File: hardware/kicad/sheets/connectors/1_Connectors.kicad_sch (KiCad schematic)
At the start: 27 parts, among them CN12 5017, CN13 B4B-PH-K-S(LF)(SN), Q68 CSD17577Q5A, U155 MT9700-N, U156 150uF, U181 LM5050MKX-1/NOPB, U81 DS1021-2x13SF11-B

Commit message: reorganized
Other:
- sheet Connectors 12V JST renamed 12V JST Outputs
- sheet Connectors 5V JST renamed 5V JST Outputs
- sheet Connectors ESC renamed ESC Connectors
- sheet Connectors Wire To Board renamed Board IO Connectors
- title: Connectors -> External Connectors
- moved on the sheet: ESC-6V1, H3, H4

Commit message: before final cleanup
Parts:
- renumbered C235 to C83, C267 to C84, C234 to C85, C274 to C86, C275 to C87, C236 to C88, CN12 to CN6, CN13 to CN7, D76 to D25, ESC-6V2 to ESC-6V1, ESC-6V1 to ESC-6V2, H3 to H5, H4 to H6, Q68 to Q14, R445 to R133, R426 to R134, R427 to R135, R514 to R136, R515 to R137, R513 to R138, U157 to U47, U155 to U48, U181 to U49, U156 to U50, U81 to U51

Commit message: pre kicad footprints
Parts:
- C84: footprint 5v rail sm-easyedapro:CAP-TH_BD13.0-P5.00-D0.6-FD -> Capacitor_THT:CP_Radial_D13.0mm_P5.00mm
- ESC-6V1: footprint 5v rail sm-easyedapro:HDR-TH_2P-P2.54-V-M -> Connector_PinHeader_2.54mm:PinHeader_2x01_P2.54mm_Vertical
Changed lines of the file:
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@@
 	(wire
 		(pts
-			(xy 101.6 64.77) (xy 142.24 64.77)
+			(xy 101.6 66.04) (xy 102.87 66.04)
 		)
 		(stroke
@@
 	(wire
 		(pts
+			(xy 100.33 97.79) (xy 142.24 97.79)
+		)
+		(stroke
+			(width 0)
+			(type default)
+		)
+	)
+	(wire
+		(pts
+			(xy 102.87 66.04) (xy 102.87 64.77)
+		)
+		(stroke
+			(width 0)
+			(type default)
+		)
+	)
+	(wire
+		(pts
 			(xy 165.1 247.65) (xy 165.1 255.27)
 		)
@@
 	(wire
 		(pts
-			(xy 101.6 97.79) (xy 142.24 97.79)
+			(xy 96.52 99.06) (xy 100.33 99.06)
 		)
 		(stroke
@@
 	(wire
 		(pts
+			(xy 100.33 99.06) (xy 100.33 97.79)
+		)
+		(stroke
+			(width 0)
+			(type default)
+		)
+	)
+	(wire
+		(pts
 			(xy 138.43 77.47) (xy 138.43 74.93)
 		)
@@
 	(wire
 		(pts
+			(xy 102.87 59.69) (xy 142.24 59.69)
+		)
+		(stroke
+			(width 0)
+			(type default)
+		)
+	)
+	(wire
+		(pts
 			(xy 105.41 200.66) (xy 100.33 200.66)
 		)
@@
 	(wire
 		(pts
-			(xy 101.6 92.71) (xy 142.24 92.71)
+			(xy 97.79 91.44) (xy 100.33 91.44)
 		)
 		(stroke
@@
 	(wire
 		(pts
-			(xy 101.6 59.69) (xy 142.24 59.69)
+			(xy 101.6 58.42) (xy 102.87 58.42)
 		)
 		(stroke
@@
 	(wire
 		(pts
+			(xy 102.87 58.42) (xy 102.87 59.69)
+		)
+		(stroke
+			(width 0)
+			(type default)
+		)
+	)
+	(wire
+		(pts
 			(xy 101.6 219.71) (xy 99.06 219.71)
 		)
@@
 	(wire
 		(pts
+			(xy 100.33 91.44) (xy 100.33 92.71)
+		)
+		(stroke
+			(width 0)
+			(type default)
+		)
+	)
+	(wire
+		(pts
 			(xy 138.43 102.87) (xy 142.24 102.87)
 		)
@@
 	(wire
 		(pts
-			(xy 101.6 95.25) (xy 142.24 95.25)
+			(xy 96.52 95.25) (xy 142.24 95.25)
 		)
 		(stroke
@@
 	(wire
 		(pts
+			(xy 102.87 64.77) (xy 142.24 64.77)
+		)
+		(stroke
+			(width 0)
+			(type default)
+		)
+	)
+	(wire
+		(pts
 			(xy 138.43 102.87) (xy 138.43 100.33)
 		)
@@
 	(wire
 		(pts
+			(xy 100.33 92.71) (xy 142.24 92.71)
+		)
+		(stroke
+			(width 0)
+			(type default)
+		)
+	)
+	(wire
+		(pts
 			(xy 151.13 247.65) (xy 151.13 255.27)
 		)
@@
 	(global_label "SBUS_RECEIVER"
 		(shape input)
-		(at 101.6 97.79 180)
+		(at 96.52 99.06 180)
 		(effects
 			(font
@@
 		)
 		(property "Intersheetrefs" "${INTERSHEET_REFS}"
-			(at 101.6 97.79 0)
+			(at 96.52 99.06 0)
 			(effects
 				(font
@@
 	(global_label "DIFF_FRONT_PWM"
 		(shape input)
-		(at 101.6 92.71 180)
+		(at 97.79 91.44 180)
 		(effects
 			(font
@@
 		)
 		(property "Intersheetrefs" "${INTERSHEET_REFS}"
-			(at 101.6 92.71 0)
+			(at 97.79 91.44 0)
 			(effects
 				(font
@@
 	(global_label "SPEED_PWM"
 		(shape input)
-		(at 101.6 64.77 180)
+		(at 101.6 66.04 180)
 		(effects
 			(font
@@
 		)
 		(property "Intersheetrefs" "${INTERSHEET_REFS}"
-			(at 101.6 64.77 0)
+			(at 101.6 66.04 0)
 			(effects
 				(font
@@
 	(global_label "THROTTLE_PWM"
 		(shape input)
-		(at 101.6 59.69 180)
+		(at 101.6 58.42 180)
 		(effects
 			(font
@@
 		)
 		(property "Intersheetrefs" "${INTERSHEET_REFS}"
-			(at 101.6 59.69 0)
+			(at 101.6 58.42 0)
 			(effects
 				(font
@@
 	(global_label "DIFF_REAR_PWM"
 		(shape input)
-		(at 101.6 95.25 180)
+		(at 96.52 95.25 180)
 		(effects
 			(font
@@
 		)
 		(property "Intersheetrefs" "${INTERSHEET_REFS}"
-			(at 101.6 95.25 0)
+			(at 96.52 95.25 0)
 			(effects
 				(font
@@
 			)
 		)
-		(property "Footprint" "5v rail sm-easyedapro:CAP-TH_BD13.0-P5.00-D0.6-FD"
+		(property "Footprint" "Capacitor_THT:CP_Radial_D13.0mm_P5.00mm"
 			(at 35.56 193.04 0)
 			(effects
@@
 			)
 		)
-		(property "Footprint" "5v rail sm-easyedapro:HDR-TH_2P-P2.54-V-M"
+		(property "Footprint" "Connector_PinHeader_2.54mm:PinHeader_2x01_P2.54mm_Vertical"
 			(at 93.98 77.47 0)
 			(effects

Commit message: imrpved footprints
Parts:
- CN7: footprint 5v rail sm-easyedapro:CONN-TH_B4B-PH-K-S -> Connector_JST:JST_PH_B4B-PH-K_1x04_P2.00mm_Vertical
- DIFF_DIFR_SBUS1, THR_STR_SPD1: footprint 5v rail sm-easyedapro:HDR-TH_9P-P2.54_C9900044301 -> Connector_PinHeader_2.54mm:PinHeader_1x09_P2.54mm_Vertical
- ESC-6V2: footprint 5v rail sm-easyedapro:HDR-TH_2P-P2.54-V-M -> Connector_PinHeader_2.54mm:PinHeader_1x02_P2.54mm_Vertical
- U51: footprint 5v rail sm-easyedapro:HDR-TH_26P-P2.54-V-M-R2-C13-S2.54 -> Connector_PinHeader_2.54mm:PinHeader_2x13_P2.54mm_Vertical
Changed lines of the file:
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@@
 			)
 		)
-		(property "Footprint" "5v rail sm-easyedapro:HDR-TH_26P-P2.54-V-M-R2-C13-S2.54"
+		(property "Footprint" "Connector_PinHeader_2.54mm:PinHeader_2x13_P2.54mm_Vertical"
 			(at 374.6246 38.1 0)
 			(effects
@@
 			)
 		)
-		(property "Footprint" "5v rail sm-easyedapro:HDR-TH_9P-P2.54_C9900044301"
+		(property "Footprint" "Connector_PinHeader_2.54mm:PinHeader_1x09_P2.54mm_Vertical"
 			(at 147.32 102.87 0)
 			(effects
@@
 			)
 		)
-		(property "Footprint" "5v rail sm-easyedapro:HDR-TH_9P-P2.54_C9900044301"
+		(property "Footprint" "Connector_PinHeader_2.54mm:PinHeader_1x09_P2.54mm_Vertical"
 			(at 147.32 69.85 0)
 			(effects
@@
 			)
 		)
-		(property "Footprint" "5v rail sm-easyedapro:CONN-TH_B4B-PH-K-S"
+		(property "Footprint" "Connector_JST:JST_PH_B4B-PH-K_1x04_P2.00mm_Vertical"
 			(at 270.51 68.58 0)
 			(effects
@@
 			)
 		)
-		(property "Footprint" "5v rail sm-easyedapro:HDR-TH_2P-P2.54-V-M"
+		(property "Footprint" "Connector_PinHeader_2.54mm:PinHeader_1x02_P2.54mm_Vertical"
 			(at 294.64 93.98 0)
 			(effects

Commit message: added better footprints and steps
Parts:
- removed C84: 4700uF, Capacitor_THT:CP_Radial_D13.0mm_P5.00mm, symbol 5v rail sm-easyedapro:ERA16V4700M13X25
- added C107: ERA16V4700M13X25, JLCImport:ERA16V4700M13X25, symbol JLCImport:ERA16V4700M13X25
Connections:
- net +SERVO_VCC: now also C107.1
- net GND: now also C107.2
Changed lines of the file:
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@@
-	)
-	(symbol
-		(lib_id "5v rail sm-easyedapro:ERA16V4700M13X25")
-		(at 35.56 193.04 270)
-		(unit 1)
-		(exclude_from_sim no)
-		(in_bom yes)
-		(on_board yes)
-		(dnp no)
-		(property "Reference" "C84"
-			(at 39.37 193.04 90)
-			(effects
-				(font
-					(size 1.27 1.27)
-				)
-				(justify left bottom)
-			)
-		)
-		(property "Value" "4700uF"
-			(at 39.37 195.58 90)
-			(effects
-				(font
-					(size 1.27 1.27)
-				)
-				(justify left bottom)
-			)
-		)
-		(property "Footprint" "Capacitor_THT:CP_Radial_D13.0mm_P5.00mm"
-			(at 35.56 193.04 0)
-			(effects
-				(font
-					(size 1.27 1.27)
-				)
-				(hide yes)
-			)
-		)
-		(property "Datasheet" "https://item.szlcsc.com/datasheet/ERA16V4700M13X25/51692194.html"
-			(at 35.56 193.04 0)
-			(effects
-				(font
-					(size 1.27 1.27)
-				)
-				(hide yes)
-			)
-		)
-		(property "Description" "Capacitance:4700uF Tolerance:±20% Tolerance:±20% Voltage Rating:16V Ripple Current:1.5A@120Hz Pin Spacing:5mm Diameter:13mm Height - Seated (Max):25mm Lifetime:2000hrs@105°C Operating Temperature:-40°C~+105°C Operating Temperature:-40°C~+105°C"
-			(at 35.56 193.04 0)
-			(effects
-				(font
-					(size 1.27 1.27)
-				)
-				(hide yes)
-			)
-		)
-		(property "Manufacturer Part" "ERA16V4700M13X25"
-			(at 35.56 193.04 0)
-			(effects
-				(font
-					(size 1.27 1.27)
-				)
-				(hide yes)
-			)
-		)
-		(property "Manufacturer" "JIERR(捷而瑞)"
-			(at 35.56 193.04 0)
-			(effects
-				(font
-					(size 1.27 1.27)
-				)
-				(hide yes)
-			)
-		)
-		(property "Supplier Part" "C49256794"
-			(at 35.56 193.04 0)
-			(effects
-				(font
-					(size 1.27 1.27)
-				)
-				(hide yes)
-			)
-		)
-		(property "Supplier" "LCSC"
-			(at 35.56 193.04 0)
-			(effects
-				(font
-					(size 1.27 1.27)
-				)
-				(hide yes)
-			)
-		)
-		(property "LCSC Part Name" "4700uF ±20% 16V"
-			(at 35.56 193.04 0)
-			(effects
-				(font
-					(size 1.27 1.27)
-				)
-				(hide yes)
-			)
-		)
-		(pin "1"
-		)
-		(pin "2"
-		)
-		(instances
-			(project "svea_powerboard_rev3"
-				(path "/3f85abf4-0b95-4c4a-b7e9-06f59ca1ea3d/5c2e021f-c2d4-49e2-8c36-9a64f1f12005/8d05c3b8-20a4-4a7f-9b20-01f8d5d5be51"
-					(reference "C84")
-					(unit 1)
-				)
-			)
-			(project "1_Connectors"
-				(path "/907d2c43-ff0f-4be5-b1b7-1b4093ecff75"
-					(reference "C?")
-					(unit 1)
-				)
-			)
-		)
 	)
 	(symbol
@@
 					(unit 1)
 				)
+			)
+		)
+	)
+	(symbol
+		(lib_id "JLCImport:ERA16V4700M13X25")
+		(at 35.56 193.04 270)
+		(unit 1)
+		(exclude_from_sim no)
+		(in_bom yes)
+		(on_board yes)
+		(dnp no)
+		(fields_autoplaced yes)
+		(property "Reference" "C107"
+			(at 39.37 191.7699 90)
+			(effects
+				(font
+					(size 1.27 1.27)
+				)
+				(justify left)
+			)
+		)
+		(property "Value" "ERA16V4700M13X25"
+			(at 39.37 194.3099 90)
+			(effects
+				(font
+					(size 1.27 1.27)
+				)
+				(justify left)
+			)
+		)
+		(property "Footprint" "JLCImport:ERA16V4700M13X25"
+			(at 35.56 193.04 0)
+			(effects
+				(font
+					(size 1.27 1.27)
+				)
+				(hide yes)
+			)
+		)
+		(property "Datasheet" "https://atta.szlcsc.com/upload/public/pdf/source/20150922/1457707409314.pdf"
+			(at 35.56 193.04 0)
+			(effects
+				(font
+					(size 1.27 1.27)
+				)
+				(hide yes)
+			)
+		)
+		(property "Description" ""
+			(at 35.56 193.04 0)
+			(effects
+				(font
+					(size 1.27 1.27)
+				)
+				(hide yes)
+			)
+		)
+		(property "LCSC" "C49256794"
+			(at 35.56 193.04 0)
+			(effects
+				(font
+					(size 1.27 1.27)
+				)
+				(hide yes)
+			)
+		)
+		(property "Manufacturer" "JIERR(捷而瑞)"
+			(at 35.56 193.04 0)
+			(effects
+				(font
+					(size 1.27 1.27)
+				)
+				(hide yes)
+			)
+		)
+		(property "Manufacturer Part" "ERA16V4700M13X25"
+			(at 35.56 193.04 0)
+			(effects
+				(font
+					(size 1.27 1.27)
+				)
+				(hide yes)
+			)
+		)
+		(pin "2"
+		)
+		(pin "1"
+		)
+		(instances
+			(project ""
+				(path "/3f85abf4-0b95-4c4a-b7e9-06f59ca1ea3d/5c2e021f-c2d4-49e2-8c36-9a64f1f12005/8d05c3b8-20a4-4a7f-9b20-01f8d5d5be51"
+					(reference "C107")
+					(unit 1)
+				)

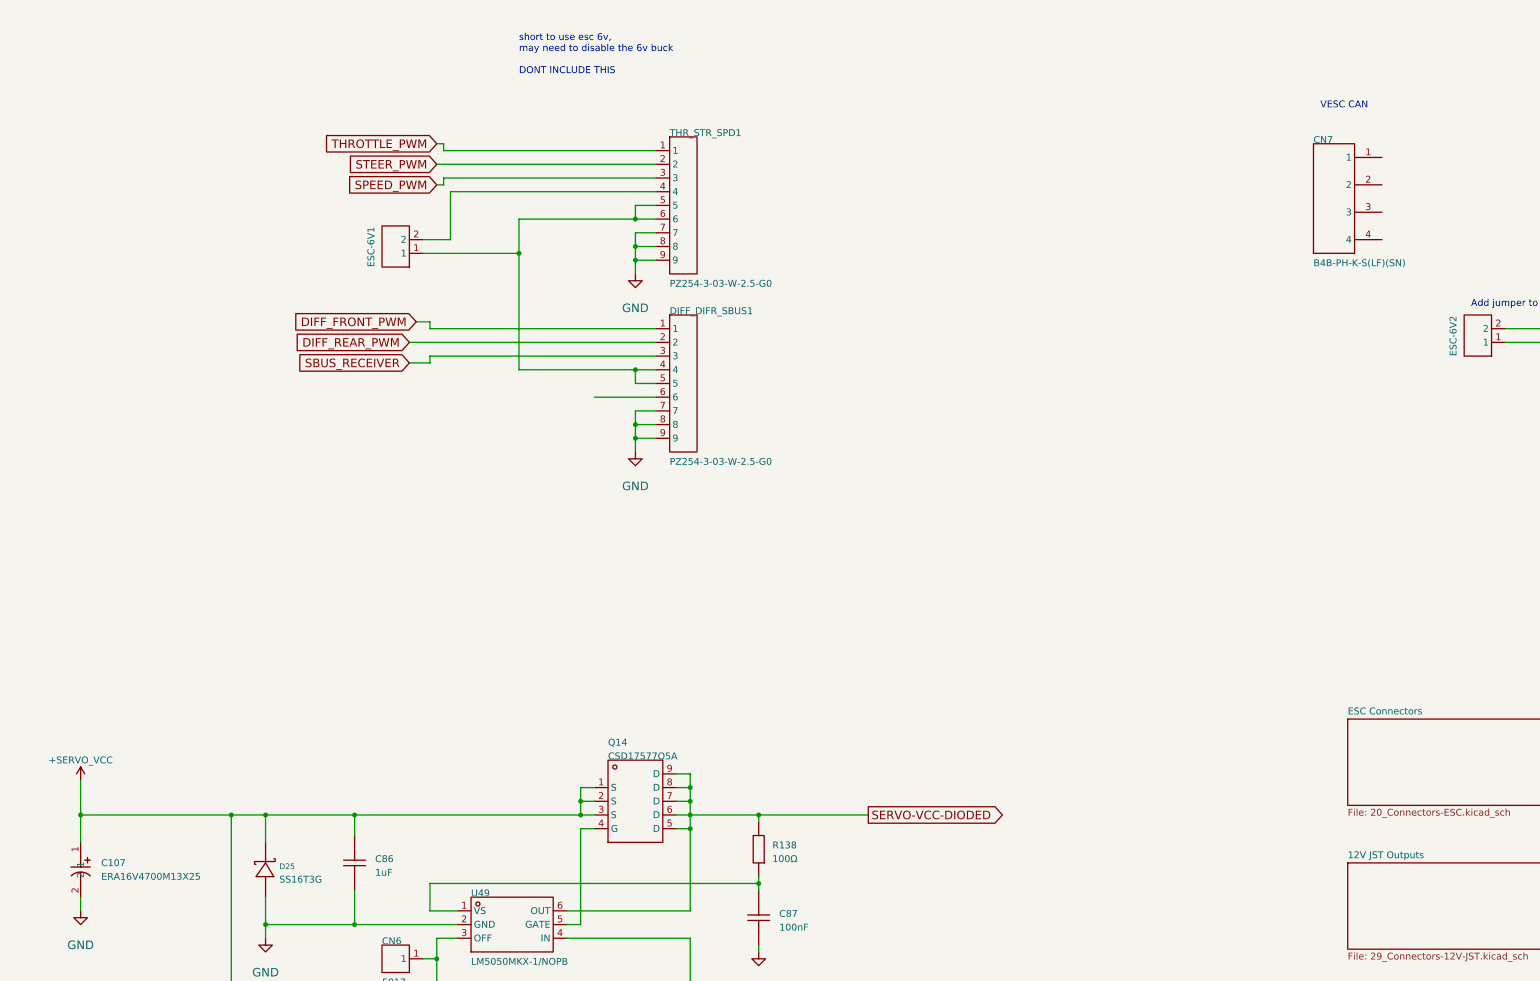
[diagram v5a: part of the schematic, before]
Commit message: better sheet nesting for power rails
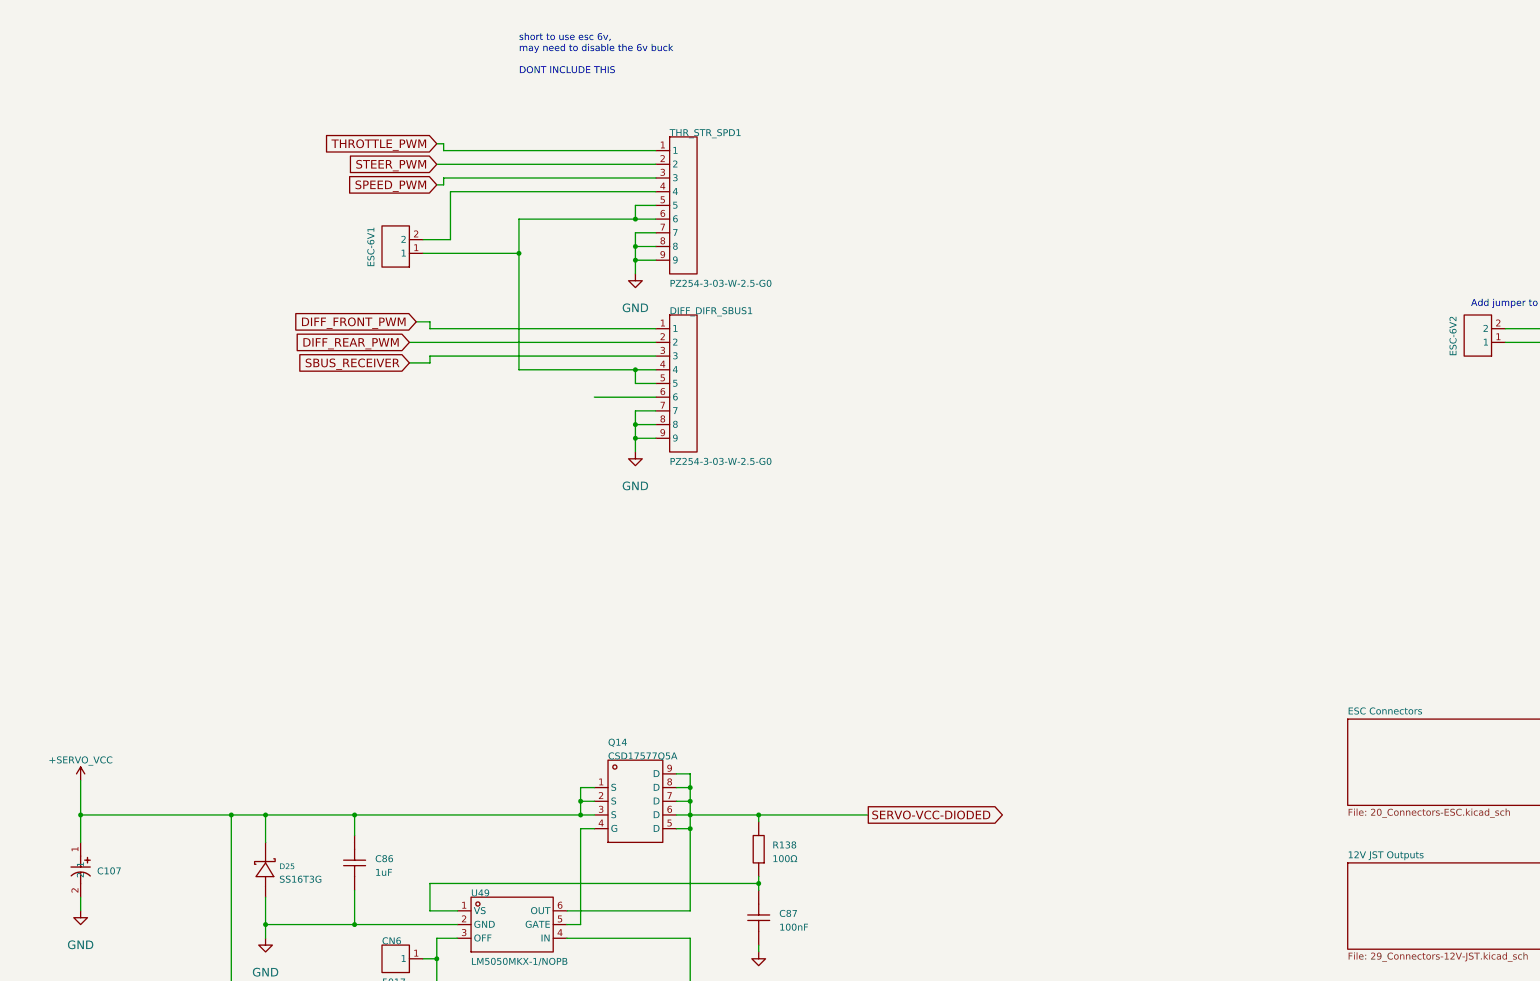
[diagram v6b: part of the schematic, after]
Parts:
- removed CN7: B4B-PH-K-S(LF)(SN), Connector_JST:JST_PH_B4B-PH-K_1x04_P2.00mm_Vertical, symbol 5v rail sm-easyedapro:B4B-PH-K-S(LF)(SN)
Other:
- note removed: "VESC CAN"
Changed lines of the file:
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@@
 		(date "2026-02-16")
 	)
-	(text "VESC CAN"
-		(exclude_from_sim no)
-		(at 265.43 52.07 0)
-		(effects
-			(font
-				(size 1.27 1.27)
-			)
-			(justify left bottom)
-		)
-	)
 	(text "600mA"
 		(exclude_from_sim no)
@@
 		(on_board yes)
 		(dnp no)
-		(fields_autoplaced yes)
 		(property "Reference" "C107"
-			(at 39.37 191.7699 90)
+			(at 38.608 193.294 90)
 			(effects
 				(font
@@
 				)
 				(justify left)
+				(hide yes)
 			)
 		)
@@
 					(unit 1)
 				)
-			)
-		)
-	)
-	(symbol
-		(lib_id "5v rail sm-easyedapro:B4B-PH-K-S(LF)(SN)")
-		(at 270.51 68.58 0)
-		(unit 1)
-		(exclude_from_sim no)
-		(in_bom yes)
-		(on_board yes)
-		(dnp no)
-		(property "Reference" "CN7"
-			(at 264.16 58.42 0)
-			(effects
-				(font
-					(size 1.27 1.27)
-				)
-				(justify left bottom)
-			)
-		)
-		(property "Value" "B4B-PH-K-S(LF)(SN)"
-			(at 264.16 81.28 0)
-			(effects
-				(font
-					(size 1.27 1.27)
-				)
-				(justify left bottom)
-			)
-		)
-		(property "Footprint" "Connector_JST:JST_PH_B4B-PH-K_1x04_P2.00mm_Vertical"
-			(at 270.51 68.58 0)
-			(effects
-				(font
-					(size 1.27 1.27)
-				)
-				(hide yes)
-			)
-		)
-		(property "Datasheet" "https://item.szlcsc.com/datasheet/B4B-PH-K-S(LF)(SN)/142627.html"
-			(at 270.51 68.58 0)
-			(effects
-				(font
-					(size 1.27 1.27)
-				)
-				(hide yes)
-			)
-		)
-		(property "Description" "Pins Structure:1x4P Pitch:2mm Mounting Type:Through Hole Reference Series:PH Number of Pins:4P Number of Rows:1 Number of PINs Per Row:4 Row Spacing:- Current Rating:2A Contact Material:Brass Contact Plating:Tin Operating Temperature:-25°C~+85°C Operating T"
-			(at 270.51 68.58 0)
-			(effects
-				(font
-					(size 1.27 1.27)
-				)
-				(hide yes)
-			)
-		)
-		(property "Manufacturer Part" "B4B-PH-K-S(LF)(SN)"
-			(at 270.51 68.58 0)
-			(effects
-				(font
-					(size 1.27 1.27)
-				)
-				(hide yes)
-			)
-		)
-		(property "Manufacturer" "JST"
-			(at 270.51 68.58 0)
-			(effects
-				(font
-					(size 1.27 1.27)
-				)
-				(hide yes)
-			)
-		)
-		(property "Supplier Part" "C131334"
-			(at 270.51 68.58 0)
-			(effects
-				(font
-					(size 1.27 1.27)
-				)
-				(hide yes)
-			)
-		)
-		(property "Supplier" "LCSC"
-			(at 270.51 68.58 0)
-			(effects
-				(font
-					(size 1.27 1.27)
-				)
-				(hide yes)
-			)
-		)
-		(property "LCSC Part Name" "1x4P 间距:2mm 直插 系列:PH"
-			(at 270.51 68.58 0)
-			(effects
-				(font
-					(size 1.27 1.27)
-				)
-				(hide yes)
-			)
-		)
-		(pin "1"
-		)
-		(pin "2"
-		)
-		(pin "3"
-		)
-		(pin "4"
-		)
-		(instances
-			(project "svea_powerboard_rev3"
-				(path "/3f85abf4-0b95-4c4a-b7e9-06f59ca1ea3d/5c2e021f-c2d4-49e2-8c36-9a64f1f12005/8d05c3b8-20a4-4a7f-9b20-01f8d5d5be51"
-					(reference "CN7")
-					(unit 1)
-				)
-			)
-			(project "1_Connectors"
-				(path "/907d2c43-ff0f-4be5-b1b7-1b4093ecff75"
-					(reference "CN?")
-					(unit 1)
-				)
